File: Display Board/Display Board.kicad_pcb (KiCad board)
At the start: 2 copper layers, 181.1 x 29.7 mm, 12 parts, among them J1 Display 1, J10 Display 1, J2 Display 2, J20 Display 2, J3 Control Board, J4 Top LED

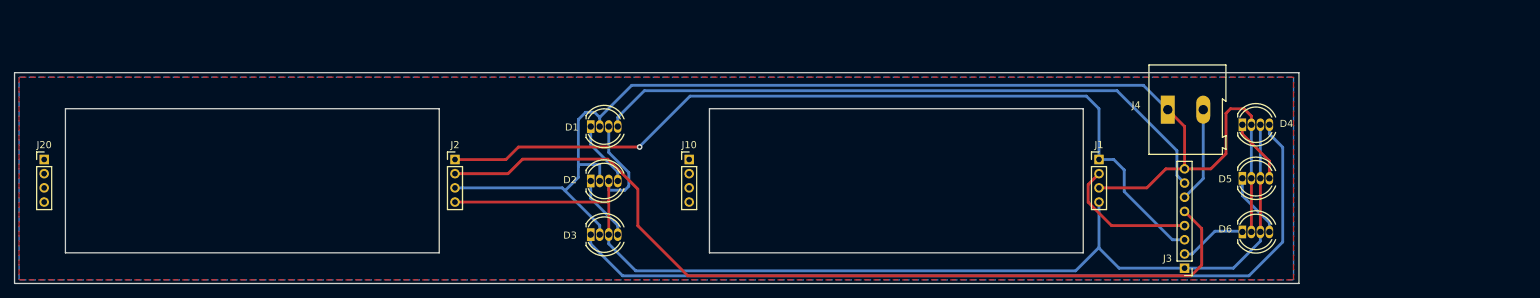
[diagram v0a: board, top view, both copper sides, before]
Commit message: working on display board and mounting
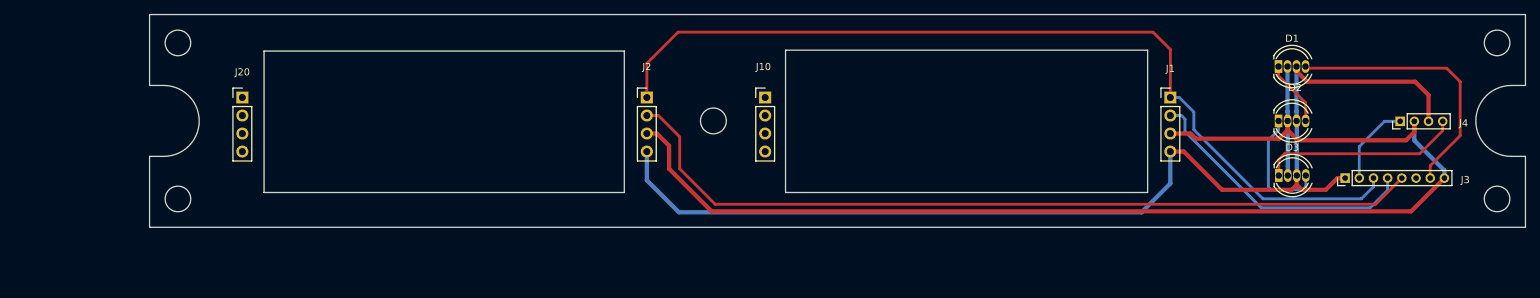
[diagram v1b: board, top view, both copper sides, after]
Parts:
- removed D4, D5, D6: APA-106-F5, LED_THT:LED_D5.0mm-4_RGB
- J1, J10, J2, J20: footprint Connector_PinHeader_2.00mm:PinHeader_1x04_P2.00mm_Vertical -> Connector_PinHeader_2.54mm:PinHeader_1x04_P2.54mm_Vertical
- J4: footprint TerminalBlock:TerminalBlock_Altech_AK300-2_P5.00mm -> Connector_PinHeader_2.00mm:PinHeader_1x04_P2.00mm_Vertical
- moved D3 97.4 mm to (239.2, 90.7)
- moved D2 97.4 mm to (239.2, 83.0)
- moved D1 97.3 mm to (239.2, 75.3)
- moved J4 32.8 mm to (256.3, 83.1), turned to 90 degrees
- moved J20 29.3 mm to (93.1, 79.7)
- moved J2 28.4 mm to (150.1, 79.7)
- moved J3 26.0 mm to (248.6, 91.1), turned to 90 degrees
- moved J10 13.8 mm to (166.8, 79.7)
- moved J1 13.3 mm to (223.9, 79.7)
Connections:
- J4 pad 1: GND -> /LED Data Out
- J4 pad 2: /TopLED -> GND
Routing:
- net Net-(D3-DO): track 120.0 -> 28.4 mm
- net /LED Data: track 90.2 -> 38.0 mm
- net /Display_1 Data: track 19.6 -> 39.8 mm
- net /TopLED: track 13.4 -> 0.00 mm
- net VCC: track 165.0 -> 155.1 mm
- net /Display_2 Data: track 125.2 -> 115.8 mm
- net Net-(D5-DO): track 9.14 -> 0.00 mm
- net Net-(D4-DO): track 9.13 -> 0.00 mm
- net Net-(D2-DO): track 9.14 -> 17.1 mm
- net /Display CLK: track 121.0 -> 126.2 mm, vias 1 -> 0
- net /LED Data Out: track 9.38 -> 11.7 mm
- net GND: track 184.2 -> 185.1 mm
- removed copper zone on B.Cu, net GND
- removed copper zone on F.Cu, net GND
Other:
- board size 181.1 x 29.7 mm -> 194 x 30 mm

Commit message: update display board with mounting holes and copper pour
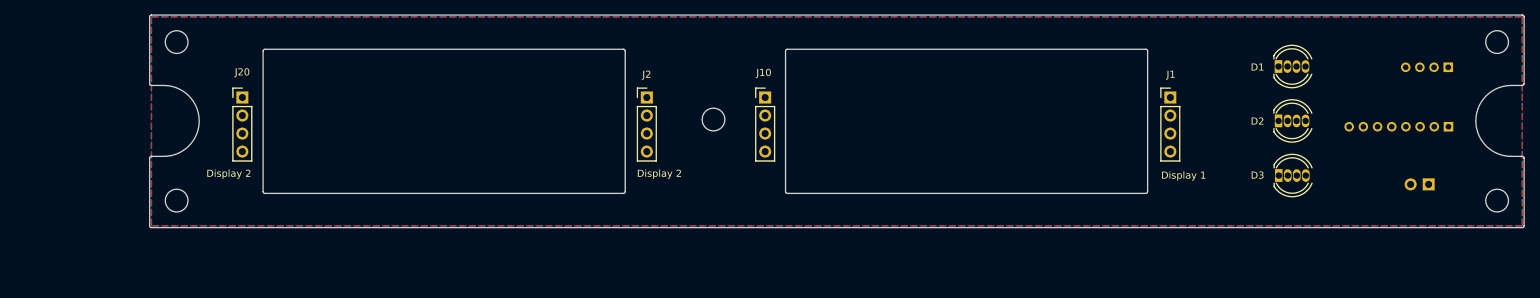
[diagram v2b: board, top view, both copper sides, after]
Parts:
- added J5: ~Flash Enable, Connector_PinHeader_2.54mm:PinHeader_1x02_P2.54mm_Vertical, B.Cu at (260.4, 91.9)
- added REF01: MountingHole_3.2mm_M3, MountingHole:MountingHole_3.2mm_M3, F.Cu at (83.8, 71.9)
- added REF02: MountingHole_3.2mm_M3, MountingHole:MountingHole_3.2mm_M3, F.Cu at (83.8, 94.2)
- added REF03: MountingHole_3.2mm_M3, MountingHole:MountingHole_3.2mm_M3, F.Cu at (159.5, 82.8)
- added REF04: MountingHole_3.2mm_M3, MountingHole:MountingHole_3.2mm_M3, F.Cu at (270.0, 94.2)
- added REF05: MountingHole_3.2mm_M3, MountingHole:MountingHole_3.2mm_M3, F.Cu at (270.0, 71.9)
- J3, J4: moved to B.Cu
- moved J3 16.3 mm to (263.1, 83.8)
- moved J4 10.2 mm to (263.1, 75.4)
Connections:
- J1 pad 2: /Display_1 Data -> Net-(J1-Pin_2)
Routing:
- net GND: track 185.1 -> 0.00 mm
- net VCC: track 155.1 -> 0.00 mm
- net /Display CLK: track 126.2 -> 0.00 mm
- net /Display_2 Data: track 115.8 -> 0.00 mm
- net /Display_1 Data: track 39.8 -> 0.00 mm
- net /LED Data: track 38.0 -> 0.00 mm
- net Net-(D3-DO): track 28.4 -> 0.00 mm
- net Net-(D2-DO): track 17.1 -> 0.00 mm
- net /LED Data Out: track 11.7 -> 0.00 mm
- net Net-(D1-DO): track 9.25 -> 0.00 mm
- added copper zone on B.Cu, net GND
- added copper zone on F.Cu, net GND
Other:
- board size 194 x 30 mm -> 193.8 x 30 mm

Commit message: re-route
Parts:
- moved D1 15.3 mm to (239.0, 90.7)
- moved D3 15.3 mm to (239.0, 75.4)
- moved J4 6.50 mm to (256.6, 75.9), turned to -90 degrees
- moved J5 6.12 mm to (254.2, 91.4), turned to -90 degrees
- moved J3 1.32 mm to (262.8, 82.5)
- moved D2 0.18 mm to (239.0, 83.0)
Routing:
- net VCC: track 0.00 -> 170.8 mm
- net GND: track 0.00 -> 155.7 mm
- net /Display_2 Data: track 0.00 -> 136.8 mm
- net /Display CLK: track 0.00 -> 133.2 mm
- net Net-(J1-Pin_2): track 0.00 -> 40.8 mm
- net Net-(D3-DO): track 0.00 -> 28.0 mm
- net /LED Data: track 0.00 -> 12.5 mm
- net Net-(D1-DO): track 0.00 -> 9.26 mm
- net Net-(D2-DO): track 0.00 -> 9.14 mm
- net /Display_1 Data: track 0.00 -> 8.89 mm
- net /LED Data Out: track 0.00 -> 8.32 mm

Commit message: v1.0-20230821
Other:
- board text added: "Control Panel Display v1.0 (20230821)"
- board text added: "remove to flash"
- board text added: "©2023 Stephen Houser, N1SH"
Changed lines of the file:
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@@
       (plot_on_all_layers_selection 0x0000000_00000000)
       (disableapertmacros false)
-      (usegerberextensions false)
-      (usegerberattributes true)
-      (usegerberadvancedattributes true)
-      (creategerberjobfile true)
+      (usegerberextensions true)
+      (usegerberattributes false)
+      (usegerberadvancedattributes false)
+      (creategerberjobfile false)
       (dashed_line_dash_ratio 12.000000)
       (dashed_line_gap_ratio 3.000000)
@@
       (psa4output false)
       (plotreference true)
-      (plotvalue true)
+      (plotvalue false)
       (plotinvisibletext false)
       (sketchpadsonfab false)
-      (subtractmaskfromsilk false)
+      (subtractmaskfromsilk true)
       (outputformat 1)
       (mirror false)
-      (drillshape 1)
+      (drillshape 0)
       (scaleselection 1)
-      (outputdirectory "")
+      (outputdirectory "gerber-20230821/")
     )
   )
@@
         (effects (font (size 1 1) (thickness 0.15)) (justify mirror))
     )
-    (fp_text value "~Flash Enable" (at 3.048 -1.016) (layer "B.SilkS")
+    (fp_text value "~Flash Enable" (at 2.798 -1.016) (layer "B.SilkS")
         (effects (font (size 1 1) (thickness 0.15)) (justify mirror))
     )
@@
   (gr_line (start 220.726 73.148) (end 220.726 92.968)
     (stroke (width 0.1) (type default)) (layer "Edge.Cuts"))
+  (gr_text "remove to flash" (at 260.5 96.25) (layer "B.SilkS")
+    (effects (font (size 1 1) (thickness 0.15)) (justify left bottom mirror))
+  )
+  (gr_text "©2023 Stephen Houser, N1SH" (at 119.5 96.5) (layer "B.SilkS")
+    (effects (font (size 1 1) (thickness 0.15)) (justify left bottom mirror))
+  )
+  (gr_text "Control Panel Display v1.0 (20230821)" (at 125.75 71.25) (layer "B.SilkS")
+    (effects (font (size 1 1) (thickness 0.15)) (justify left bottom mirror))
+  )
   (segment (start 242.824 85.568) (end 242.824 83) (width 0.4) (layer "B.Cu") (net 1))
   (segment (start 239.014 89.378) (end 242.824 85.568) (width 0.4) (layer "B.Cu") (net 1))
